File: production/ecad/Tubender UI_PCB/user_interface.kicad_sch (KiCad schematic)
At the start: 11 parts, among them IC3 SN74LVC1G29DCTR, J1 640387-5, J2 1-640387-0, U5 74HC595, U6 PEC11R-4215K-S0024

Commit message: More FootyPrints
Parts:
- C10, C11, C18: footprint (none) -> Capacitor_SMD:C_0805_2012Metric
- DS1: footprint DIPS1524W50P254L3760H835Q12N -> (none)
- IC3: footprint SOP65P400X130-8N -> (none)
- J1: footprint 640387-5:TE_640387-5 -> footprints:TE_640387-5
- J2: footprint 1-640387-0:TE_1-640387-0 -> footprints:TE_1-640387-0
- R20, R22: footprint (none) -> Resistor_SMD:R_0805_2012Metric
- U6: footprint PEC11R-4XXXK-SXXXX -> (none)
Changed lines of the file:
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@@
 			)
 		)
-		(property "Footprint" "640387-5:TE_640387-5"
+		(property "Footprint" "footprints:TE_640387-5"
 			(at 224.79 109.22 0)
 			(effects
@@
 			)
 		)
-		(property "Footprint" ""
+		(property "Footprint" "Capacitor_SMD:C_0805_2012Metric"
 			(at 36.5252 38.1 0)
 			(effects
@@
 			)
 		)
-		(property "Footprint" "SOP65P400X130-8N"
+		(property "Footprint" ""
 			(at 128.27 -39.04 0)
 			(effects
@@
 			)
 		)
-		(property "Footprint" ""
+		(property "Footprint" "Resistor_SMD:R_0805_2012Metric"
 			(at 232.41 48.26 0)
 			(effects
@@
 			)
 		)
-		(property "Footprint" ""
+		(property "Footprint" "Resistor_SMD:R_0805_2012Metric"
 			(at 232.41 53.34 0)
 			(effects
@@
 			)
 		)
-		(property "Footprint" ""
+		(property "Footprint" "Capacitor_SMD:C_0805_2012Metric"
 			(at 234.95 58.42 0)
 			(effects
@@
 			)
 		)
-		(property "Footprint" "1-640387-0:TE_1-640387-0"
+		(property "Footprint" "footprints:TE_1-640387-0"
 			(at 62.23 114.3 0)
 			(effects
@@
 			)
 		)
-		(property "Footprint" ""
+		(property "Footprint" "Capacitor_SMD:C_0805_2012Metric"
 			(at 243.84 58.42 0)
 			(effects
@@
 			)
 		)
-		(property "Footprint" "DIPS1524W50P254L3760H835Q12N"
+		(property "Footprint" ""
 			(at 109.22 143.18 0)
 			(effects
@@
 			)
 		)
-		(property "Footprint" "PEC11R-4XXXK-SXXXX"
+		(property "Footprint" ""
 			(at 224.79 143.18 0)
 			(effects

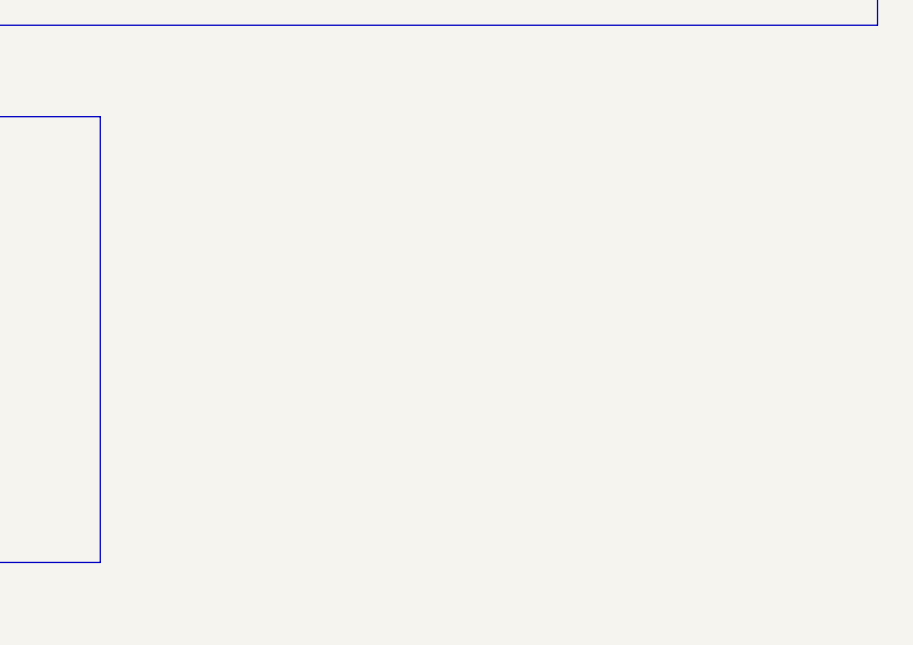
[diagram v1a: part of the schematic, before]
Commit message: Added SD card reader
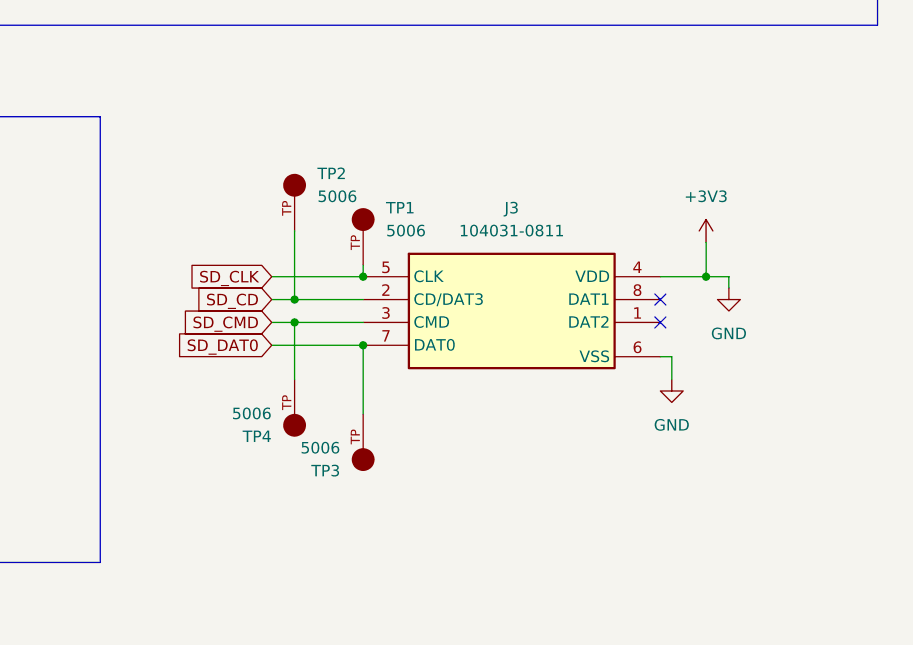
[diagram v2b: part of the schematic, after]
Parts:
- added J3: 104031-0811, 1040310811, symbol 104031-0811:104031-0811
- added TP1, TP2, TP3, TP4: 5006, 5006:KEYSTONE_5006, symbol 5006:5006
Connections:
- net GND is gone; now on net +3V3: C10.2, C11.2, C18.2, IC3.4 (GND), J1.5, J2.10, U5.8 (GND), U6.5 (C)
- net +3V3: now also J3.4 (VDD), J3.6 (VSS)
- new net SD_CD: J3.2 (CD/DAT3), TP2.TP
- new net SD_CLK: J3.5 (CLK), TP1.TP
- new net SD_CMD: J3.3 (CMD), TP4.TP
- new net SD_DAT0: J3.7 (DAT0), TP3.TP
- no-connect marks 4 -> 6

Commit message: Some intial work for rotary encoder on  PCB
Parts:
- U6: footprint (none) -> Rotary_Encoder:SW_PEC11R-4XXXK-SXXXX_BRN
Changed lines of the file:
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@@
 			)
 		)
-		(property "Footprint" ""
+		(property "Footprint" "Rotary_Encoder:SW_PEC11R-4XXXK-SXXXX_BRN"
 			(at 224.79 143.18 0)
 			(effects
